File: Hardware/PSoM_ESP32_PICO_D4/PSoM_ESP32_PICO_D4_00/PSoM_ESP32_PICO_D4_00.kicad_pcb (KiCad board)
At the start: 6 copper layers, 26.3 x 23.2 mm, 58 parts, among them J101 DF40C-60DP-0.4V(51), J102 Bare PCB USB C, SW401 SW_Push, SW402 SW_Push, U201 BQ24075RGTR, U301 MIC5528-3.3YMT-T5, U401 ESP32-S2FH4, Y601 Crystal_GND24_Small

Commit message: First route for the PICO_D4
Added .gitignore
Modify at your own taste, this one will be tricky
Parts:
- removed the C401 at (127.8, 92.4)
- removed the C402 at (127.8, 95.6)
- removed the C403 at (130.0, 95.8)
- removed C408, C411, C412, C415, C416: 100n, Capacitor_SMD:C_0201_0603Metric
- removed C409: 10u, Capacitor_SMD:C_0603_1608Metric
- removed C410, C413: 1u, Capacitor_SMD:C_0402_1005Metric
- removed G***: LOGO, Component_lib:puma_logo_14mm
- removed J102: Bare PCB USB C, Component_lib:usb-c-pcb
- removed R101, R102: 5.1k, Resistor_SMD:R_0201_0603Metric
- removed the R401 at (131.5, 92.9)
- removed R404: 10k, Resistor_SMD:R_0201_0603Metric
- removed R405, R406, R407: nu, Resistor_SMD:R_0201_0603Metric
- removed Y601: Crystal_GND24_Small, Component_lib:Crystal_SMD_2016-4Pin_2.0x1.6mm
- added R409: nu, Resistor_SMD:R_0201_0603Metric, B.Cu at (129.6, 102.7)
- C401: renamed from C404; value 100n -> 10u
- R408: moved to B.Cu
- U401: value ESP32-S2FH4 -> ESP32-PICO-D4; footprint Component_lib:QFN40P700X700X90-57N-D -> Components_NdG:ESP32-PICO-D4_1
- moved R408 7.25 mm to (134.9, 103.0), turned to 180 degrees
- moved C402 0.92 mm to (130.7, 93.3)
- moved R202 0.28 mm to (142.3, 98.1)
- moved R201 0.27 mm to (143.3, 98.1)
- moved C203 0.16 mm to (139.1, 93.5)
- moved R204 0.11 mm to (140.6, 95.7)
- renumbered C405 to C402, C406 to C403, C407 to C404, C414 to C405, R402 to R401, R403 to R402, SW402 to SW401, SW401 to SW402
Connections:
- net /400_ESP32/LNA_IN renamed /400_ESP32/LAN_IN
- C101 pad 1: IO1 -> IO39
- J101 pad 11: IO5 -> IO18
- J101 pad 13: IO6 -> IO19
- J101 pad 15: IO7 -> IO21
- J101 pad 17: IO8 -> IO34
- J101 pad 19: IO9 -> IO32
- J101 pad 21: IO10 -> IO33
- J101 pad 23: IO11 -> IO35
- J101 pad 25: IO12 -> IO36
- J101 pad 27: IO13 -> IO37
- J101 pad 29: IO14 -> IO38
- J101 pad 30: IO33 -> unconnected-(J101-Pad30)
- J101 pad 31: IO15 -> unconnected-(J101-Pad31)
- J101 pad 32: IO34 -> unconnected-(J101-Pad32)
- J101 pad 33: IO16 -> unconnected-(J101-Pad33)
- J101 pad 34: IO35 -> IO5
- J101 pad 35: IO17 -> IO25
- J101 pad 36: IO36 -> IO15
- J101 pad 37: IO18 -> IO26
- J101 pad 38: IO37 -> IO12
- J101 pad 39: IO21 -> unconnected-(J101-Pad39)
- J101 pad 40: IO38 -> IO9
- J101 pad 42: IO41 -> IO22
- J101 pad 43: SPI7 -> unconnected-(J101-Pad43)
- J101 pad 44: IO39 -> IO23
- J101 pad 46: IO40 -> IO27
- J101 pad 5: IO2 -> IO4
- J101 pad 52: IO42 -> unconnected-(J101-Pad52)
- J101 pad 56: /100_Connectors/D+ -> unconnected-(J101-Pad56)
- J101 pad 58: /100_Connectors/D- -> unconnected-(J101-Pad58)
- J101 pad 7: IO3 -> IO13
- J101 pad 9: IO4 -> IO14
- R103 pad 2: IO1 -> IO39
- R104 pad 1: IO1 -> IO39
- R401 pad 1: IO15 -> IO2
- R408 pad 1: /400_ESP32/IO45 -> IO15
- U401 pad 10: IO5 -> IO34
- U401 pad 11: IO6 -> IO35
- U401 pad 12: IO7 -> IO32
- U401 pad 13: IO8 -> IO33
- U401 pad 14: IO9 -> IO25
- U401 pad 15: IO10 -> IO26
- U401 pad 16: IO11 -> IO27
- U401 pad 17: IO12 -> IO14
- U401 pad 18: IO13 -> IO12
- U401 pad 19: IO14 -> +3V3
- U401 pad 20: +3V3 -> IO13
- U401 pad 22: IO16 -> IO2
- U401 pad 23: IO17 -> IO0
- U401 pad 24: IO18 -> IO4
- U401 pad 25: /100_Connectors/D- -> unconnected-(U401-GPIO16-Pad25)
- U401 pad 26: /100_Connectors/D+ -> SPI6
- U401 pad 27: +3V3 -> SPI1
- U401 pad 28: IO21 -> IO9
- U401 pad 29: SPI7 -> SPI3
- U401 pad 30: SPI6 -> SPI5
- U401 pad 31: SPI5 -> SPI2
- U401 pad 33: SPI3 -> SPI0
- U401 pad 34: SPI2 -> IO5
- U401 pad 35: SPI1 -> IO18
- U401 pad 36: SPI0 -> IO23
- U401 pad 37: IO33 -> +3V3
- U401 pad 38: IO34 -> IO19
- U401 pad 39: IO35 -> IO22
- U401 pad 40: IO36 -> /100_Connectors/TX0
- U401 pad 41: IO37 -> /100_Connectors/RX0
- U401 pad 42: IO38 -> IO21
- U401 pad 43: IO39 -> +3V3
- U401 pad 44: IO40 -> unconnected-(U401-NC-Pad44)
- U401 pad 45: +3V3 -> unconnected-(U401-NC-Pad45)
- U401 pad 46: IO41 -> +3V3
- U401 pad 47: IO42 -> unconnected-(U401-CAP2-Pad47)
- U401 pad 48: /100_Connectors/TX0 -> unconnected-(U401-CAP1-Pad48)
- U401 pad 49: /100_Connectors/RX0 -> GND
- U401 pad 5: IO0 -> IO36
- U401 pad 6: IO1 -> IO37
- U401 pad 7: IO2 -> IO38
- U401 pad 8: IO3 -> IO39
- U401 pad 9: IO4 -> /100_Connectors/EN
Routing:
- net GND: track 96.0 -> 62.6 mm, vias 71 -> 44
- net VBUS: track 48.9 -> 17.8 mm, vias 5 -> 2
- net +3V3: track 36.4 -> 14.8 mm, vias 13 -> 7
- net /100_Connectors/D-: track 21.5 -> 0.00 mm, vias 3 -> 0
- net /100_Connectors/D+: track 20.4 -> 0.00 mm, vias 2 -> 0
- net IO22: track 0.00 -> 18.7 mm
- net IO41: track 17.8 -> 0.00 mm
- net IO40: track 17.6 -> 0.00 mm
- net IO23: track 0.00 -> 16.3 mm, vias 0 -> 2
- net IO42: track 15.3 -> 0.00 mm, vias 2 -> 0
- net IO35: track 15.0 -> 0.00 mm
- net IO33: track 15.0 -> 0.00 mm
- net IO34: track 15.1 -> 0.28 mm
- net IO3: track 13.5 -> 0.00 mm
- net IO6: track 11.8 -> 0.00 mm
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- removed copper zone on In2.Cu, net +3V3
- removed copper zone on B.Cu, net GND
- removed copper zone on F.Cu, net GND
- removed copper zone on In4.Cu, net GND

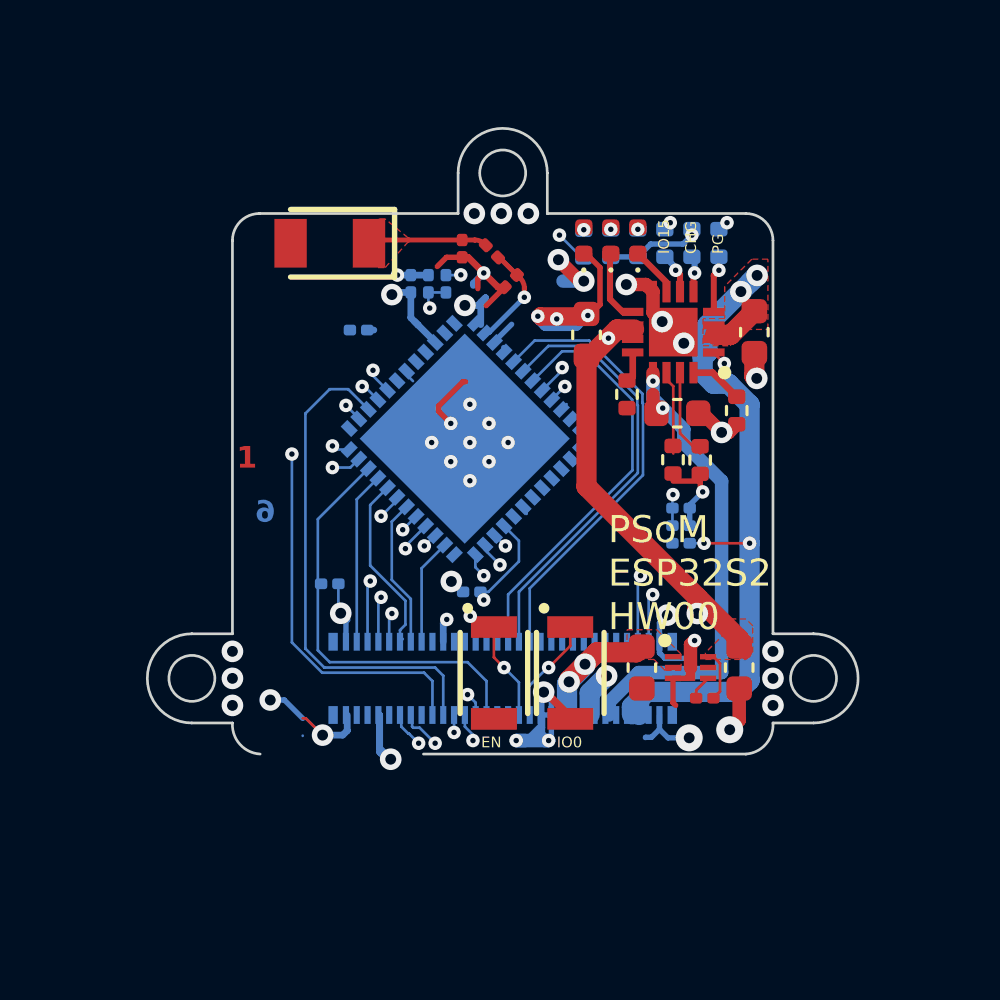
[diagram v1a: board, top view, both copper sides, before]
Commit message: IO routes finished
Still missing the routes for GND and 3.3V
Tried to adjust the .gitignore, experimental
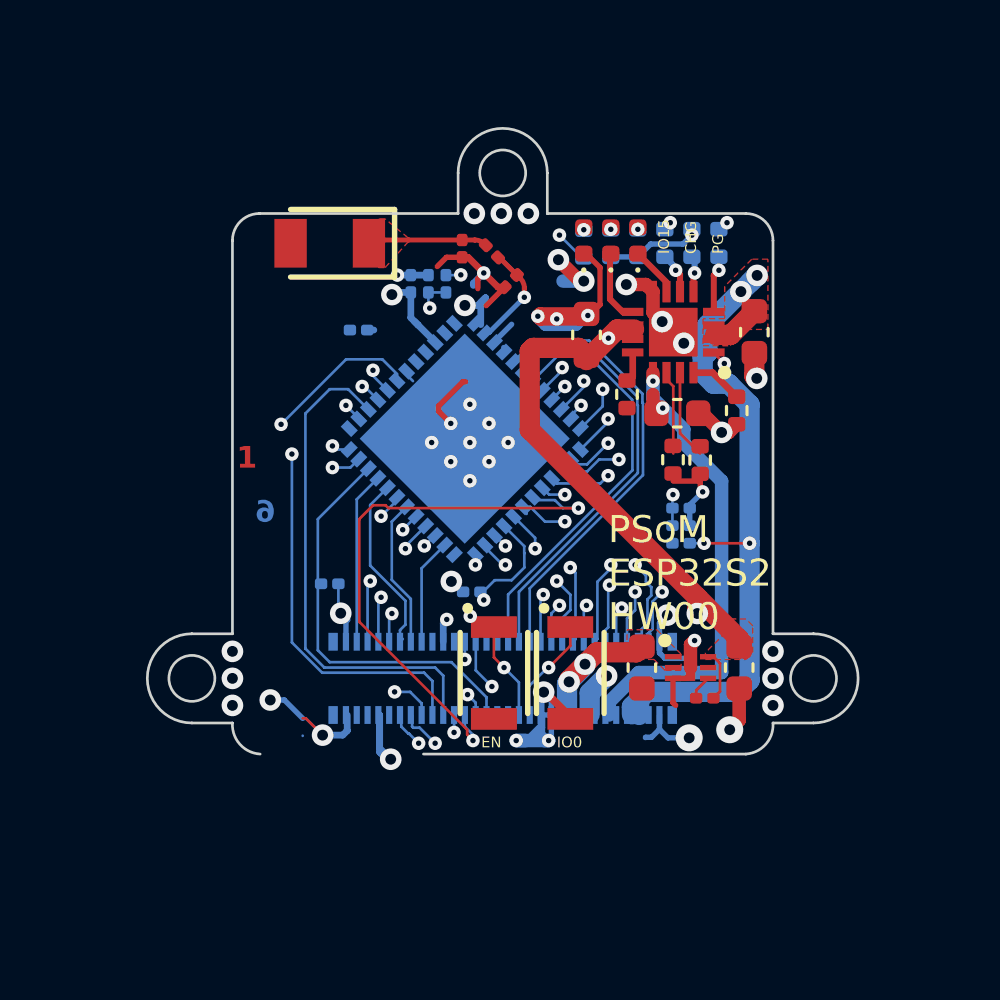
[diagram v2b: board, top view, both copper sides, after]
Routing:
- net IO27: track 0.00 -> 28.8 mm, vias 0 -> 2
- net IO21: track 0.00 -> 25.1 mm, vias 0 -> 2
- net IO25: track 0.31 -> 21.0 mm, vias 0 -> 2
- net IO12: track 1.07 -> 21.2 mm, vias 1 -> 2
- net IO26: track 0.00 -> 19.1 mm, vias 0 -> 2
- net IO19: track 0.70 -> 17.4 mm, vias 1 -> 2
- net IO18: track 1.11 -> 17.3 mm, vias 1 -> 2
- net IO32: track 0.00 -> 14.0 mm, vias 0 -> 2
- net IO34: track 0.28 -> 13.3 mm, vias 0 -> 2
- net IO33: track 0.00 -> 12.3 mm, vias 0 -> 2
- net IO35: track 0.00 -> 10.9 mm, vias 0 -> 2
- net IO13: track 0.03 -> 9.40 mm, vias 0 -> 2
- net IO14: track 0.00 -> 7.68 mm, vias 0 -> 2
- net /VSYS: track 38.3 -> 41.8 mm
- net SPI1: track 5.39 -> 8.44 mm
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
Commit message: Officially finished first version of PicoD4 PSoM
Modified .gitignore
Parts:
- C405, R402: moved to F.Cu
- moved R402 7.58 mm to (138.8, 97.4), turned to 180 degrees
- moved C405 7.52 mm to (138.8, 96.7), turned to 0 degrees
- moved C402 2.80 mm to (132.9, 91.6), turned to 90 degrees
- moved C401 1.01 mm to (133.6, 91.6)
- moved C203 0.27 mm to (139.1, 93.2)
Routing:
- net +3V3: track 16.5 -> 55.5 mm, vias 8 -> 9
- net GND: track 62.6 -> 68.8 mm, vias 44 -> 42
- net /100_Connectors/EN: track 24.8 -> 19.3 mm, vias 4 -> 3
- net IO12: track 21.2 -> 15.9 mm
- net /VSYS: track 41.8 -> 37.5 mm
- net IO9: track 11.8 -> 10.8 mm
- net VBUS: track 17.8 -> 18.3 mm
- added copper zone on In4.Cu, net GND
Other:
- outline, holes or cut-outs redrawn

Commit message: pico d4 routage terminé?
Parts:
- C401: footprint Capacitor_SMD:C_0201_0603Metric -> Capacitor_SMD:C_0603_1608Metric
- U401: footprint Components_NdG:ESP32-PICO-D4_1 -> Component_lib:ESP32-PICO-D4_1
- moved C301 15.3 mm to (134.3, 94.6), turned to -45 degrees
- moved U301 14.0 mm to (133.1, 95.8), turned to 45 degrees
- moved R301 13.5 mm to (135.9, 95.7), turned to -135 degrees
- moved C302 12.8 mm to (131.8, 97.1), turned to -45 degrees
- moved C405 10.4 mm to (133.3, 105.5), turned to 180 degrees
- moved R402 9.21 mm to (133.3, 104.8), turned to 0 degrees
- moved C402 1.38 mm to (132.4, 92.9), turned to 135 degrees
- moved C401 0.76 mm to (132.9, 91.9), turned to 135 degrees
- moved C203 0.56 mm to (139.1, 92.7)
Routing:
- net GND: track 68.8 -> 41.9 mm, vias 42 -> 46
- net /300_Power/PRIM_LDO_EN: track 0.91 -> 3.91 mm
- net IO27: track 28.8 -> 26.7 mm
- net IO12: track 15.9 -> 14.1 mm
- net +3V3: track 55.5 -> 53.7 mm, vias 9 -> 7
- net /VBAT: track 26.9 -> 25.3 mm
- net /VSYS: track 37.5 -> 39.1 mm, vias 4 -> 6
- net IO23: track 16.8 -> 15.4 mm
- net IO4: track 11.7 -> 12.9 mm
- net IO33: track 12.3 -> 13.4 mm
- net IO32: track 14.0 -> 13.2 mm
- net IO36: track 16.8 -> 17.5 mm
- net IO22: track 18.7 -> 18.0 mm
- net IO25: track 21.0 -> 20.4 mm
- net /100_Connectors/RX0: track 18.7 -> 18.1 mm
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- added copper zone on B.Cu, net GND
- added copper zone on F.Cu, net GND
- added copper zone on In2.Cu, net GND
- added copper zone on In3.Cu, net GND
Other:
- board text added: "IO2"
- board text added: "PSoM ESP32D4 HW00"
- board text removed: "IO15"
- board text removed: "PSoM ESP32S2 HW00"
